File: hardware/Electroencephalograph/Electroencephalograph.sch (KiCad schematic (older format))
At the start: 0 parts

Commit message: further routing
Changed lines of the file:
@@
 $EndDescr
 $Sheet
-S 1300 1200 650  250
+S 1300 1300 650  250
 U 5DF4CFF8
 F0 "EEGFrontendElectrode1To4" 50
@@
 $EndSheet
 $Sheet
-S 1300 1800 500  150
+S 1300 1900 500  150
 U 5E312944
 F0 "EEGFrontendElectrode5To8" 50
@@
 $EndSheet
 $Sheet
-S 2050 2600 500  150
+S 6100 1600 500  150
 U 5E27E78E
 F0 "ComputerInterface" 50

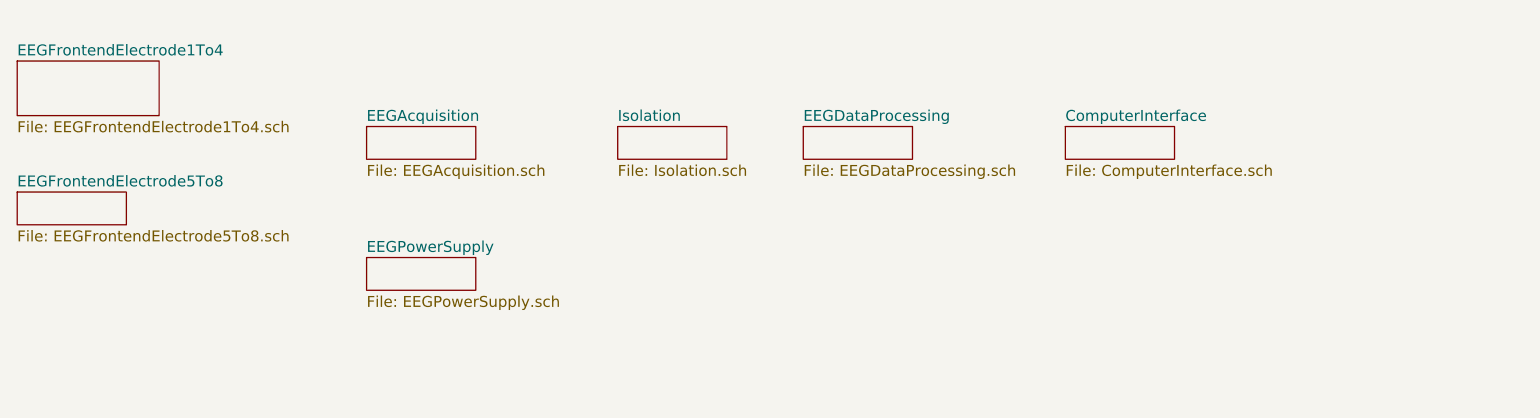
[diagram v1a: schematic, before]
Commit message: placement of usb interface, fix in grounds
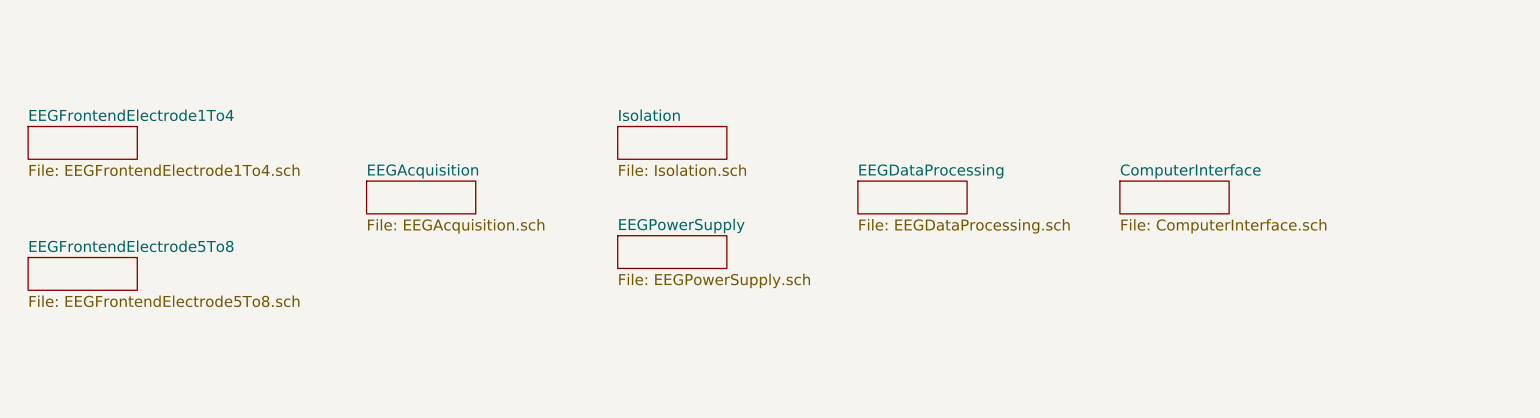
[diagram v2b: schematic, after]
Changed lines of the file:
@@
 encoding utf-8
 Sheet 1 8
-Title ""
+Title "Main sheet"
 Date ""
-Rev ""
-Comp ""
-Comment1 ""
+Rev "1.0"
+Comp "MIT License"
+Comment1 "Links to all to all sheets in project"
 Comment2 ""
 Comment3 ""
@@
 $EndDescr
 $Sheet
-S 1300 1300 650  250
+S 1350 1600 500  150
 U 5DF4CFF8
 F0 "EEGFrontendElectrode1To4" 50
@@
 $EndSheet
 $Sheet
-S 2900 1600 500  150
+S 2900 1850 500  150
 U 5DF61103
 F0 "EEGAcquisition" 50
@@
 $EndSheet
 $Sheet
-S 4900 1600 500  150
+S 5150 1850 500  150
 U 5E142744
 F0 "EEGDataProcessing" 50
@@
 $EndSheet
 $Sheet
-S 2900 2200 500  150
+S 4050 2100 500  150
 U 5E0992D6
 F0 "EEGPowerSupply" 50
@@
 $EndSheet
 $Sheet
-S 1300 1900 500  150
+S 1350 2200 500  150
 U 5E312944
 F0 "EEGFrontendElectrode5To8" 50
@@
 $EndSheet
 $Sheet
-S 6100 1600 500  150
+S 6350 1850 500  150
 U 5E27E78E
 F0 "ComputerInterface" 50

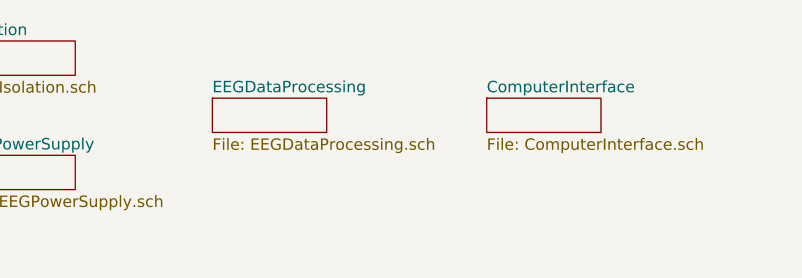
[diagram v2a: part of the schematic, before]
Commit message: fix #41, fix #18
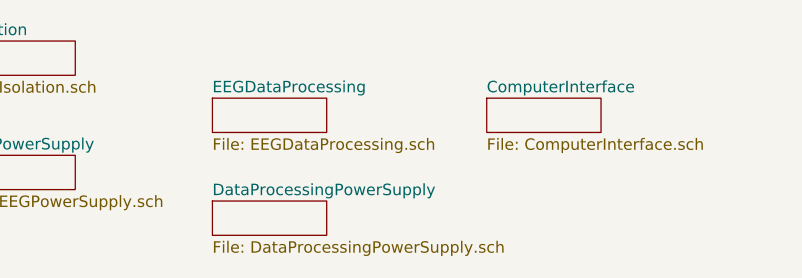
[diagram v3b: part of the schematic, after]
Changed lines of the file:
@@
 $Descr A4 11693 8268
 encoding utf-8
-Sheet 1 8
+Sheet 1 9
 Title "Main sheet"
 Date ""
@@
 F1 "ComputerInterface.sch" 50
 $EndSheet
+$Sheet
+S 5150 2300 500  150
+U 5EC8DA4D
+F0 "DataProcessingPowerSupply" 50
+F1 "DataProcessingPowerSupply.sch" 50
+$EndSheet
 $EndSCHEMATC

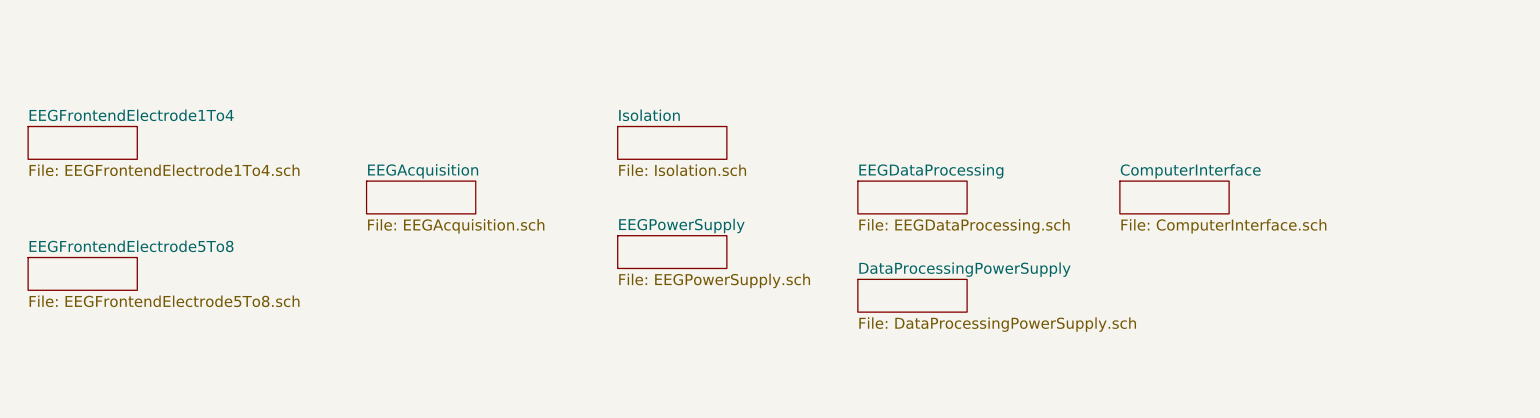
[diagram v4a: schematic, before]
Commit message: split user interface to separate sheets
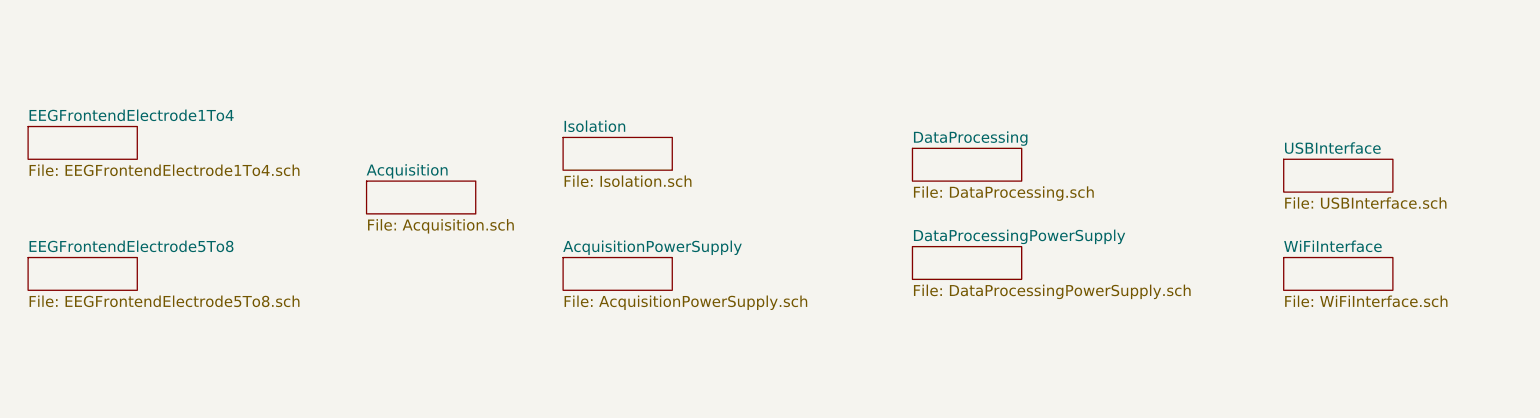
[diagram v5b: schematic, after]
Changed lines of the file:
@@
 $Descr A4 11693 8268
 encoding utf-8
-Sheet 1 9
+Sheet 1 10
 Title "Main sheet"
 Date ""
@@
 S 2900 1850 500  150
 U 5DF61103
-F0 "EEGAcquisition" 50
-F1 "EEGAcquisition.sch" 50
+F0 "Acquisition" 50
+F1 "Acquisition.sch" 50
 $EndSheet
 $Sheet
-S 5150 1850 500  150
+S 5400 1700 500  150
 U 5E142744
-F0 "EEGDataProcessing" 50
-F1 "EEGDataProcessing.sch" 50
+F0 "DataProcessing" 50
+F1 "DataProcessing.sch" 50
 $EndSheet
 $Sheet
-S 4050 1600 500  150
+S 3800 1650 500  150
 U 5DFE0AD6
 F0 "Isolation" 50
@@
 $EndSheet
 $Sheet
-S 4050 2100 500  150
+S 3800 2200 500  150
 U 5E0992D6
-F0 "EEGPowerSupply" 50
-F1 "EEGPowerSupply.sch" 50
+F0 "AcquisitionPowerSupply" 50
+F1 "AcquisitionPowerSupply.sch" 50
 $EndSheet
 $Sheet
@@
 $EndSheet
 $Sheet
-S 6350 1850 500  150
+S 7100 1750 500  150
 U 5E27E78E
-F0 "ComputerInterface" 50
-F1 "ComputerInterface.sch" 50
+F0 "USBInterface" 50
+F1 "USBInterface.sch" 50
 $EndSheet
 $Sheet
-S 5150 2300 500  150
+S 5400 2150 500  150
 U 5EC8DA4D
 F0 "DataProcessingPowerSupply" 50
 F1 "DataProcessingPowerSupply.sch" 50
 $EndSheet
+$Sheet
+S 7100 2200 500  150
+U 5F01FBEA
+F0 "WiFiInterface" 50
+F1 "WiFiInterface.sch" 50
+$EndSheet
 $EndSCHEMATC
